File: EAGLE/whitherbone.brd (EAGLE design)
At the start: 86.4 x 54.6 mm, 227 parts, among them IC10 TXS0108ERGYR, IC11 TXS0108ERGYR, IC12 TPS2051BDGN, IC13 SN74AUC1G74, IC14 TPD4S012DRY, IC15 TPD4S012DRY, IC17 SN74LVC2G241DCUR, IC18 TL1963ADCQR, IC19 AP2112K-1.8TRG1 3.3V, IC2 SN74LVC1G07DCK, IC4 7805T, IC7 IP4283CZ10-TBR, IC8 IP4283CZ10-TBR, IC9 TDA19988BHN/C1,557, J1 1-1747981-1, Q2 32.768kHz, Q4 24 MHz, T1 BSS138W-7-F, T3 BSS138W-7-F, T4 BSS138W-7-F, U1 OSD3358-512M-BSM, U2 A3967SLBTR, X2 SCHA5B0200, X4 10118192-0001LF

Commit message: Some minor power fixups
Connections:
- removed net SYS_VDD_1P8V: U1.F10, U1.G10, U1.H10, U1.H11, U1.J10, U1.J11, U1.K10, U1.L10
- net N$22: now also U1.M16
- net VDD_1V8: now also U1.F10, U1.G10, U1.H10, U1.H11, U1.J10, U1.J11, U1.K10, U1.L10
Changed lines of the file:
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@@
 <wire x1="28.067" y1="9.2964" x2="28.067" y2="17.6276" width="0.254" layer="3"/>
 <wire x1="28.067" y1="17.6276" x2="28.575" y2="18.1356" width="0.254" layer="3"/>
-<wire x1="56.896" y1="21.463" x2="58.039" y2="20.066" width="0" layer="19" extent="1-1"/>
+<contactref element="U1" pad="H10"/>
+<contactref element="U1" pad="H11"/>
+<contactref element="U1" pad="J10"/>
+<contactref element="U1" pad="K10"/>
+<contactref element="U1" pad="L10"/>
+<contactref element="U1" pad="F10"/>
+<contactref element="U1" pad="G10"/>
+<contactref element="U1" pad="J11"/>
+<wire x1="53.1368" y1="73.7616" x2="51.8668" y2="73.7616" width="0" layer="19" extent="1-1"/>
+<wire x1="51.8668" y1="72.4916" x2="51.8668" y2="73.7616" width="0" layer="19" extent="1-1"/>
+<wire x1="53.1368" y1="72.4916" x2="53.1368" y2="73.7616" width="0" layer="19" extent="1-1"/>
+<wire x1="54.4068" y1="72.4916" x2="53.1368" y2="72.4916" width="0" layer="19" extent="1-1"/>
+<wire x1="55.6768" y1="72.4916" x2="54.4068" y2="72.4916" width="0" layer="19" extent="1-1"/>
+<wire x1="50.5968" y1="72.4916" x2="51.8668" y2="72.4916" width="0" layer="19" extent="1-1"/>
+<wire x1="49.3268" y1="72.4916" x2="50.5968" y2="72.4916" width="0" layer="19" extent="1-1"/>
+<wire x1="45.466" y1="27.686" x2="49.3268" y2="72.4916" width="0" layer="19" extent="1-1"/>
+<wire x1="58.039" y1="20.066" x2="56.896" y2="21.463" width="0" layer="19" extent="1-1"/>
 </signal>
 <signal name="N$11" class="1">
@@
 <wire x1="60.706" y1="11.176" x2="61.476" y2="11.176" width="0.1524" layer="16"/>
 <via x="60.706" y="11.176" extent="1-16" drill="0.4064"/>
+<contactref element="U1" pad="M16"/>
+<wire x1="60.706" y1="11.176" x2="56.9468" y2="80.1116" width="0" layer="19" extent="1-16"/>
 </signal>
 <signal name="SD.CD">
@@
 <wire x1="55.6768" y1="69.9516" x2="54.4068" y2="69.9516" width="0" layer="19" extent="1-1"/>
 </signal>
-<signal name="SYS_VDD_1P8V">
-<contactref element="U1" pad="F10"/>
-<contactref element="U1" pad="G10"/>
-<contactref element="U1" pad="H10"/>
-<contactref element="U1" pad="H11"/>
-<contactref element="U1" pad="J10"/>
-<contactref element="U1" pad="J11"/>
-<contactref element="U1" pad="K10"/>
-<contactref element="U1" pad="L10"/>
-<wire x1="50.5968" y1="72.4916" x2="49.3268" y2="72.4916" width="0" layer="19" extent="1-1"/>
-<wire x1="51.8668" y1="72.4916" x2="50.5968" y2="72.4916" width="0" layer="19" extent="1-1"/>
-<wire x1="53.1368" y1="72.4916" x2="51.8668" y2="72.4916" width="0" layer="19" extent="1-1"/>
-<wire x1="51.8668" y1="73.7616" x2="51.8668" y2="72.4916" width="0" layer="19" extent="1-1"/>
-<wire x1="53.1368" y1="73.7616" x2="53.1368" y2="72.4916" width="0" layer="19" extent="1-1"/>
-<wire x1="54.4068" y1="72.4916" x2="53.1368" y2="72.4916" width="0" layer="19" extent="1-1"/>
-<wire x1="55.6768" y1="72.4916" x2="54.4068" y2="72.4916" width="0" layer="19" extent="1-1"/>
-</signal>
 <signal name="VDDSHV1">

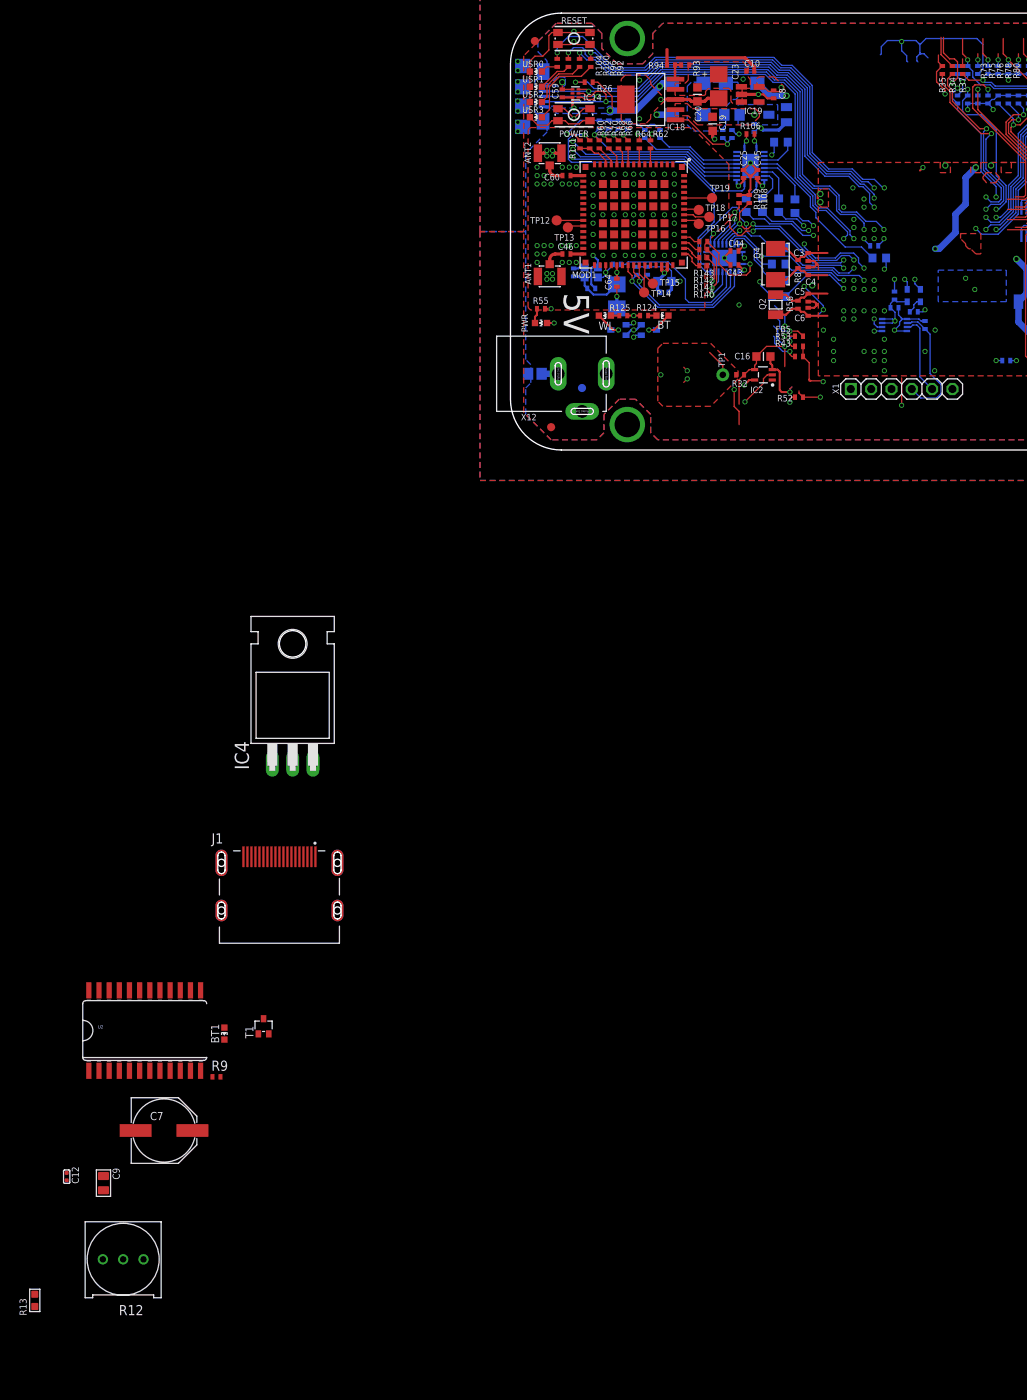
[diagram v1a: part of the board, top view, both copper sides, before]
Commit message: Move WiFi signals to 1.8V and remove level shifters
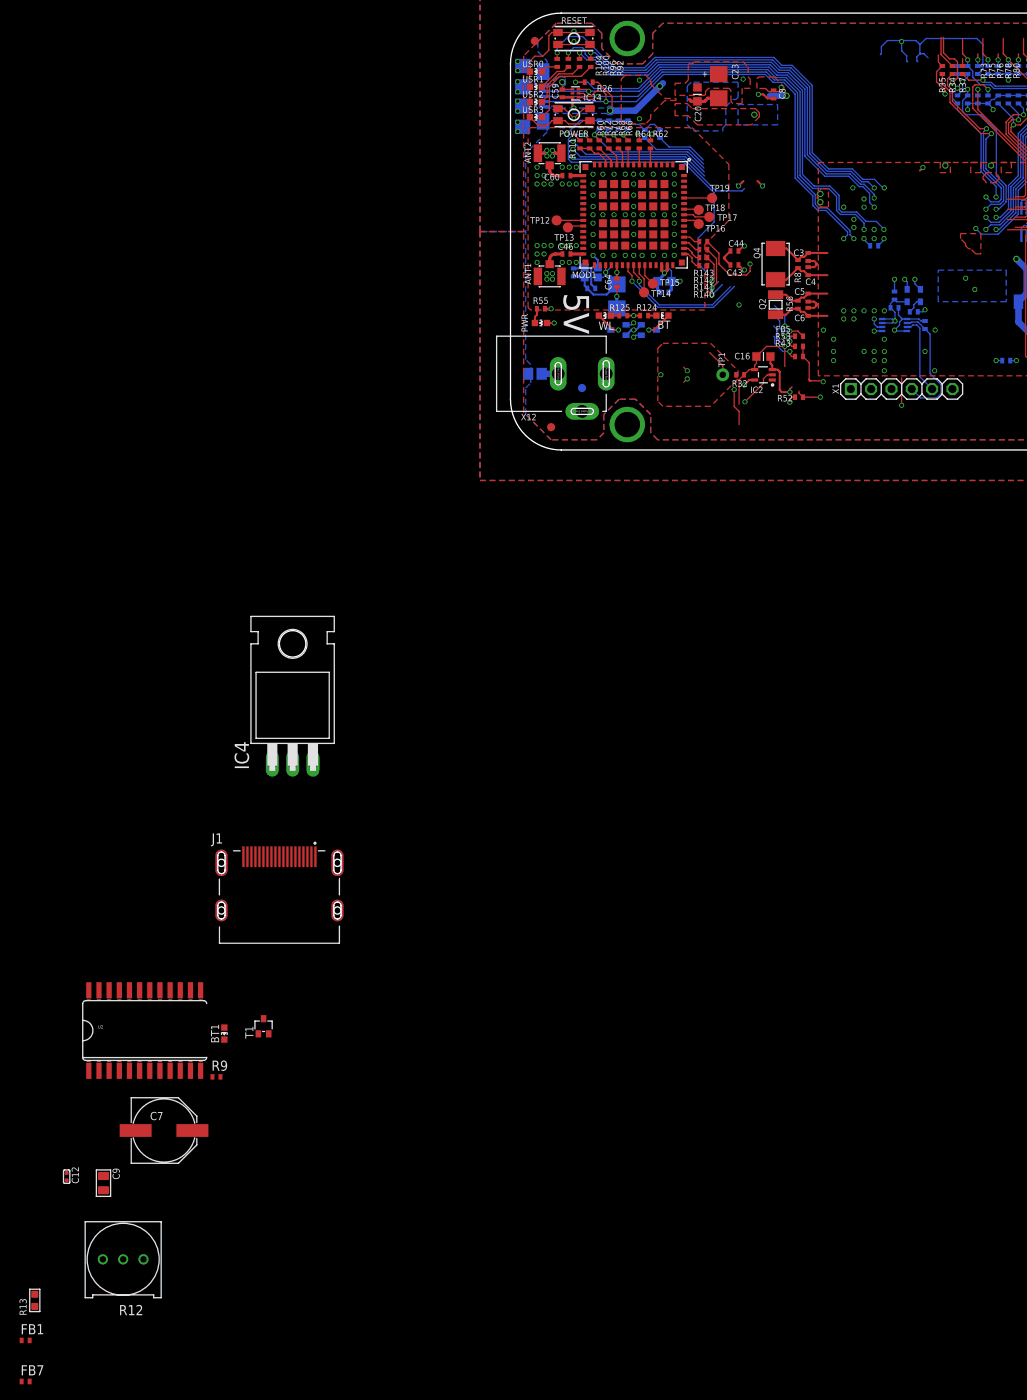
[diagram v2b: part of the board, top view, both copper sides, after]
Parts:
- removed C10: 1uF, rcl:C0402K
- removed C19: 10uF, 6.3V, rcl:C0603K
- removed C25, C45: .1uF, 6.3V, rcl:C0402K
- removed D2: STPS140A DNP, GHI:DIODE_SMA
- removed D3, D4: STPS140A, GHI:DIODE_SMA
- removed D8: BAT54C, diode:SOT23
- removed IC10, IC11: TXS0108ERGYR, GHI-IC:R-PVQFN-N20(TI)
- removed IC18: TL1963ADCQR, GHI-IC:SOT-223(DCQ_R-PDSO-G6_TI)
- removed IC19: AP2112K-1.8TRG1 3.3V, GHI:SOT23-5
- removed R10, R11: 150k, rcl:R0402
- removed R106: 1.5k, rcl:R0402
- removed R108, R109, R97: DNP 1k, rcl:R0402
- removed R126, R127, R128, R129, R130, R131, R134, R135, R136, R86: 33, 5%, rcl:R0603
- removed R89: 1k, rcl:R0402
- removed R91: 0 DNP, rcl:R0402
- removed R93: 7.15k, rcl:R0402
- removed R94: 4.12k, rcl:R0402
- removed R95: 1M, rcl:R0402
- removed TP23: PTR1B1,27, testpad:B1,27
- added FB7: 1k BLM15AG102SN1D, rcl:R0402
- FB1: value 220 Ohm 800mA -> 1k BLM15AG102SN1D; device GHI-BasicComponents:0805-RESISTOR -> rcl:R0402
- moved FB1 176.8 mm to (-60.6, -111.3), flipped to the top, turned to 0 degrees
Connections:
- removed net 5V_IN: C19.1, D8.3, FB1.2, IC18.2, R95.1
- removed net ALT.BT.EN: IC11.17, R135.2
- removed net ALT.BUFF.OE: IC10.10, IC11.10, R106.1, R131.1
- removed net ALT.WL.CLK: IC10.15, R126.2
- removed net ALT.WL.CMD: IC10.14, R86.2
- removed net ALT.WL.D0: IC10.20, R130.2
- removed net ALT.WL.D1: IC10.18, R129.2
- removed net ALT.WL.D2: IC10.17, R128.2
- removed net ALT.WL.D3: IC10.16, R127.2
- removed net ALT.WL.EN: IC11.18, R136.2
- removed net ALT.WL.IRQ: IC11.12, R134.2
- removed net BT_EN.SIP: R135.1, U1.H15
- removed net BT_HCI_CTS.SIP: IC11.15, R108.1, U1.E13
- removed net BT_HCI_RTS.SIP: IC11.13, R109.1, U1.D13
- removed net BT_HCI_RX.SIP: IC11.14, U1.D14
- removed net BT_HCI_TX.SIP: IC11.20, U1.D15
- removed net CLKOUT2: IC11.16
- removed net LS_BUF_OE: R131.2, U1.E16
- removed net N$30: R9.2
- removed net N$9: IC18.5, R93.2, R94.1
- removed net SELECT_5V: D2.K, D3.K, D4.K, FB1.1, R97.1, TP23.TP
- removed net SLOW_CLK: IC11.5, R91.1
- removed net VDDSHV1: U1.J9
- removed net VDDSHV2: U1.K9
- removed net VDDSHV3: U1.L9
- removed net VDDSHV4: U1.F9
- removed net VDDSHV5: U1.G9
- removed net VDDSHV6: U1.H9
- removed net WL_EN.SIP: R136.1, U1.H16
- removed net WL_IRQ.SIP: R134.1, U1.H14
- removed net WL_SDIO_CLK.SIP: R126.1, U1.D16
- removed net WL_SDIO_CMD.SIP: R86.1, U1.G14
- removed net WL_SDIO_D0.SIP: R130.1, U1.F16
- removed net WL_SDIO_D1.SIP: R129.1, U1.G15
- removed net WL_SDIO_D2.SIP: R128.1, U1.G16
- removed net WL_SDIO_D3.SIP: R127.1, U1.F15
- new net VDD_3V3A: U1.F9, U1.H8, U1.H9, U1.J7, U1.J8, U1.J9, U1.K8, U1.K9, U1.L8, U1.L9
- net 1.8V-WIFI: now also FB7.1; no longer C25.1, IC10.2, IC11.2, IC19.5
- net 3.3V-WIFI: now also FB1.1, R9.2; no longer C10.1, C45.1, IC10.19, IC11.19, IC18.4, IC19.1, IC19.3, R93.1
- net 32.768KHZ: no longer R91.2
- net BT_EN: now also U1.H15; no longer IC11.4, R11.1
- net BT_HCI_CTS: now also U1.E13; no longer IC11.8
- net BT_HCI_RTS: now also U1.D13; no longer IC11.6
- net BT_HCI_RX: now also U1.D14; no longer IC11.1
- net BT_HCI_TX: now also U1.D15; no longer IC11.7
- net GND: no longer C10.2, C19.2, C25.2, C45.2, D8.2, IC10.11, IC10.TP, IC11.11, IC11.TP, IC18.3, IC18.6, IC19.2, R10.2, R106.2, R108.2, R109.2, R11.2, R94.2, R95.2
- net N$5: now also U1.D6, U1.D7; no longer IC18.1, R89.2, R97.2
- net SYS_5V: no longer D2.A
- net SYS_VDD3_3P3V: no longer U1.H8, U1.J7, U1.J8, U1.K8, U1.L8
- net USB_DC: no longer D4.A
- net VDD_1V8: now also FB7.2, U1.G9
- net VDD_3V3B: now also FB1.2; no longer R89.1
- net VDD_5V: no longer D3.A
- net WL_EN: now also U1.H16; no longer IC11.3, R10.1
- net WL_IRQ: now also U1.H14; no longer IC11.9
- net WL_SDIO_CLK: now also U1.D16; no longer IC10.6
- net WL_SDIO_CMD: now also U1.G14; no longer IC10.7
- net WL_SDIO_D0: now also U1.F16; no longer IC10.1
- net WL_SDIO_D1: now also U1.G15; no longer IC10.3
- net WL_SDIO_D2: now also U1.G16; no longer IC10.4
- net WL_SDIO_D3: now also U1.F15; no longer IC10.5
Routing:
- net VDD_5V: track 85.8 -> 0.00 mm, vias 4 -> 0
- net CLKOUT2: track 60.2 -> 0.00 mm, vias 3 -> 0
- net GND: track 226.7 -> 185.1 mm, vias 142 -> 136
- net ALT.BUFF.OE: track 37.5 -> 0.00 mm, vias 2 -> 0
- net BT_HCI_RTS.SIP: track 25.6 -> 0.00 mm, vias 3 -> 0
- net WL_SDIO_CMD.SIP: track 24.7 -> 0.00 mm, vias 2 -> 0
- net BT_HCI_RX.SIP: track 24.5 -> 0.00 mm, vias 3 -> 0
- net BT_HCI_CTS.SIP: track 23.9 -> 0.00 mm, vias 3 -> 0
- net WL_SDIO_D0.SIP: track 21.3 -> 0.00 mm, vias 2 -> 0
- net WL_SDIO_D1.SIP: track 19.7 -> 0.00 mm, vias 2 -> 0
- net SLOW_CLK: track 19.6 -> 0.00 mm
- net ALT.WL.CLK: track 19.5 -> 0.00 mm
- net BT_HCI_TX.SIP: track 19.3 -> 0.00 mm, vias 3 -> 0
- net WL_SDIO_D2.SIP: track 18.1 -> 0.00 mm, vias 2 -> 0
- net WL_SDIO_D3.SIP: track 16.2 -> 0.00 mm, vias 2 -> 0
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
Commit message: Copied BigEasyDriver
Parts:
- removed U2: A3967SLBTR, A3967SLBTR:SOIC24WIDE
- added C10, C13, C14, C15, C18: .1uf, SparkFun:0402-CAP
- added C17: .22uF, SparkFun:0402-CAP
- added FB8: 1k BLM15AG102SN1D, rcl:R0402
- added IC1: A4983, SparkFun:QFN-28-5MM
- added JP3: (no value), SparkFun:1X04
- added JP5: (no value), BigEasyDriver_v11:SCREWTERMINAL-3.5MM-4_LOCK
- added R10, R18: .11, SparkFun:R2010
- added R11, R14, R15, R20, R21, R22, R23: 20K, SparkFun:0402-RES
- added R16: 10K, SparkFun:TRIMPOT-3MM
- added R25: 2.49K, SparkFun:0402-RES
- added TP2: TPPAD1-13, testpad:P1-13
- R12: value 10K -> 20K; device Seeed-Resistor:ADJR3-9.5X9.5X10.5MM -> SparkFun:0402-RES
- R13: value 2K -> 20K; device Seeed-Resistor:R0603 -> SparkFun:0402-RES
- moved R12 53.1 mm to (-38.5, -153.3)
- moved R13 52.8 mm to (-35.4, -153.3)
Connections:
- new net COILA+: IC1.P$21, JP3.4, JP5.4
- new net COILA-: IC1.P$24, JP3.3, JP5.3
- new net COILB+: IC1.P$1, JP3.1, JP5.1
- new net COILB-: IC1.P$26, JP3.2, JP5.2
- new net CUR_REF: IC1.P$17, R16.2, TP2.TP
- new net DIR: IC1.P$19, R22.1
- new net ENABLE: IC1.P$2, R21.1
- new net MS1: IC1.P$9, R11.1
- new net MS2: IC1.P$10, R12.1
- new net MS3: IC1.P$11, R13.1
- new net MVCC: C13.1, IC1.P$15, R11.2, R12.2, R13.2, R14.2, R15.2, R22.2, R23.2, R25.1
- new net N$30: IC1.P$13, R20.1
- new net N$32: IC1.P$23, R10.2
- new net N$46: C17.1, IC1.P$8
- new net N$47: C18.1, IC1.P$6
- new net N$48: R16.1, R25.2
- new net N$9: C10.1, IC1.P$4
- new net RESET: IC1.P$12, R15.1
- new net SLEEP: IC1.P$14, R14.1
- new net STEP: IC1.P$16, R23.1
- net 12VDC: now also C14.1, C15.1, C18.2, IC1.P$22, IC1.P$28
- net GND: now also C13.2, C14.2, C15.2, C17.2, IC1.P$18, IC1.P$29, IC1.P$3, R10.1, R16.3, R18.1, R20.2, R21.2; no longer R13.1, U2.18, U2.19, U2.6, U2.7
- net N$10: now also C10.2, IC1.P$5; no longer R12.3, U2.1
- net N$31: now also IC1.P$27, R18.2; no longer R12.1, R13.2
- net VDD_5V: no longer R12.2, U2.14
